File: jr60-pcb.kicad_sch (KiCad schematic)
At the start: 21 parts, among them J1 AVR-ISP-6, SW1 SW_Push, U1 ATmega32U4-A, U2 PRTR5V0U2X, X1 XTAL

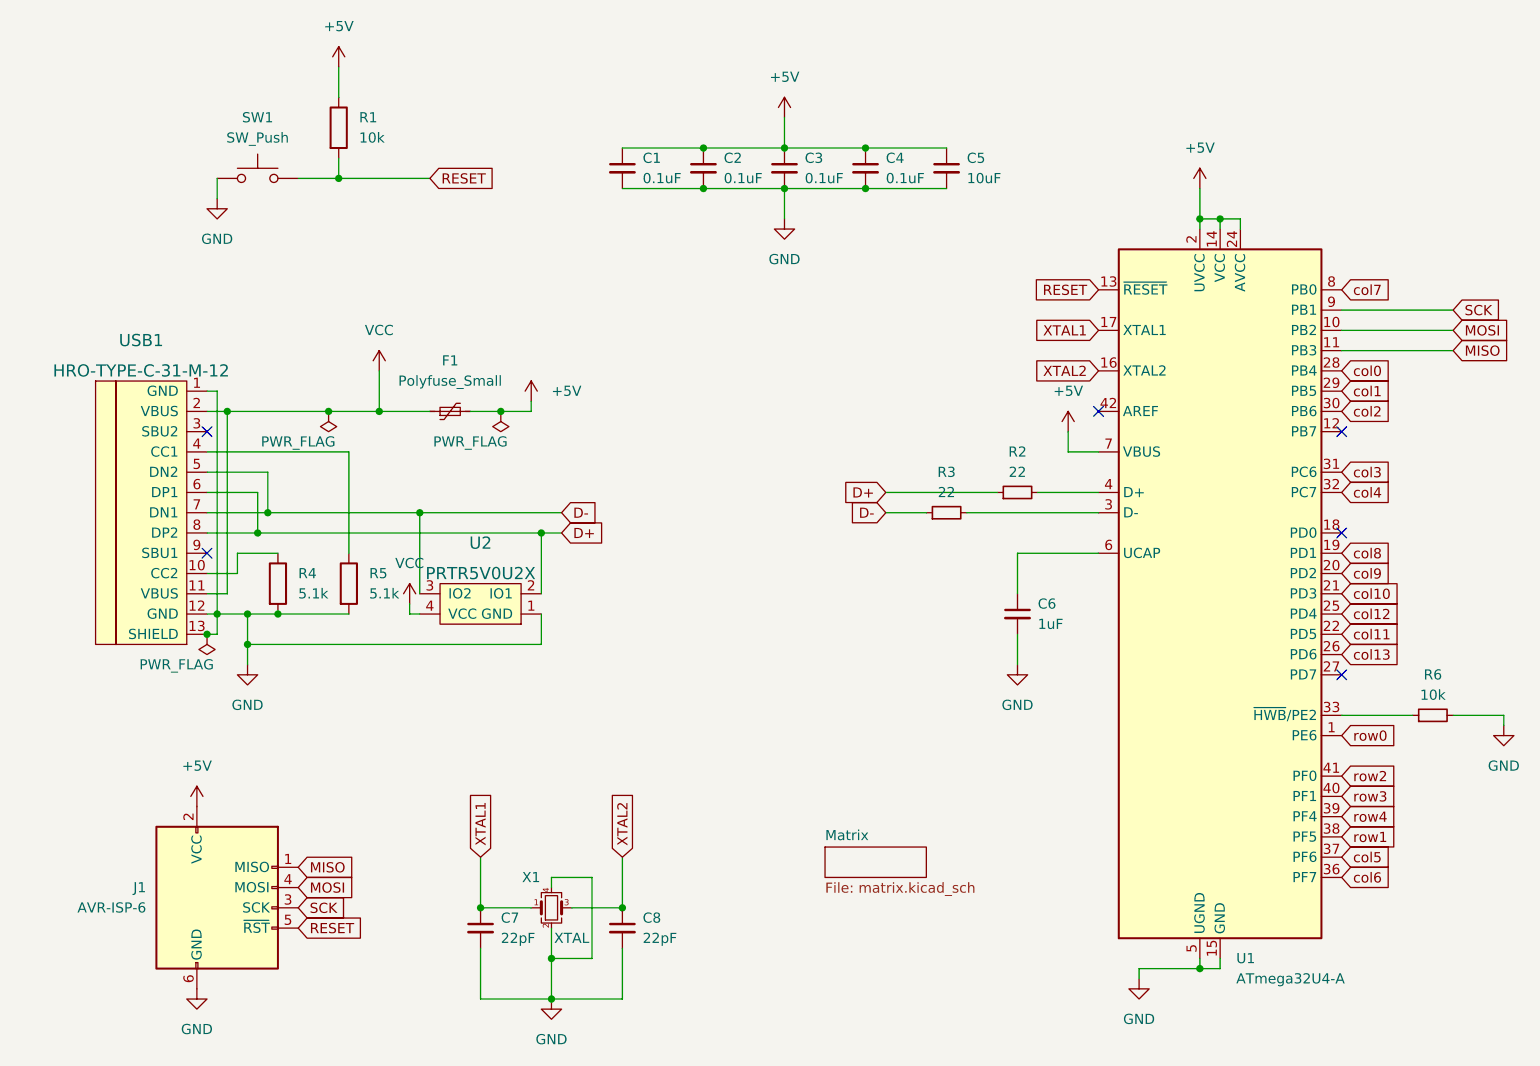
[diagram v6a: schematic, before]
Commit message: added all traces
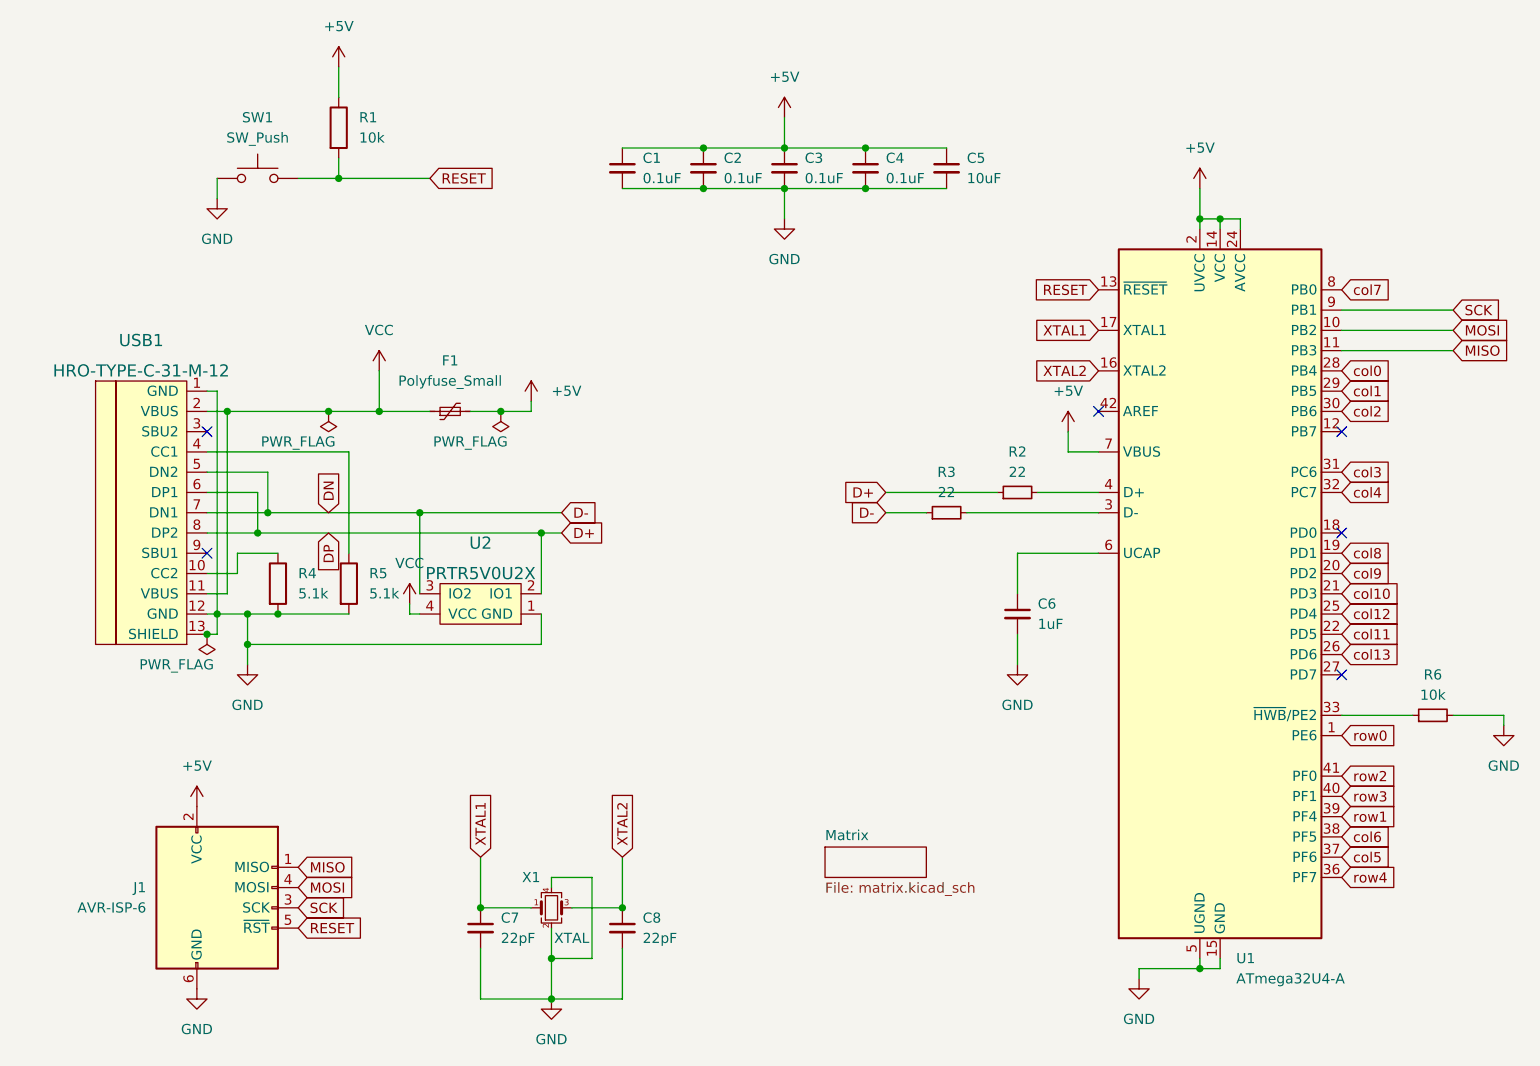
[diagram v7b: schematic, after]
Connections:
- net col6: now also U1.38 (PF5); no longer U1.36 (PF7)
- net row1: now also U1.39 (PF4); no longer U1.38 (PF5)
- net row4: now also U1.36 (PF7); no longer U1.39 (PF4)
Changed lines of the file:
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@@
     (stroke (width 0) (type default) (color 0 0 0 0))
   )
+  (global_label "DN" (shape input) (at 128.27 95.25 90) (fields_autoplaced)
+    (effects (font (size 1.27 1.27)) (justify left))
+    (property "Intersheet References" "${INTERSHEET_REFS}" (id 0) (at 128.1906 90.2364 90)
+      (effects (font (size 1.27 1.27)) (justify left) hide)
+    )
+  )
   (global_label "col5" (shape input) (at 255.27 138.43 0) (fields_autoplaced)
     (effects (font (size 1.27 1.27)) (justify left))
@@
     )
   )
-  (global_label "row4" (shape input) (at 255.27 133.35 0) (fields_autoplaced)
+  (global_label "row1" (shape input) (at 255.27 133.35 0) (fields_autoplaced)
     (effects (font (size 1.27 1.27)) (justify left))
     (property "Intersheet References" "${INTERSHEET_REFS}" (id 0) (at 262.1583 133.2706 0)
@@
     )
   )
-  (global_label "row1" (shape input) (at 255.27 135.89 0) (fields_autoplaced)
-    (effects (font (size 1.27 1.27)) (justify left))
-    (property "Intersheet References" "${INTERSHEET_REFS}" (id 0) (at 262.1583 135.8106 0)
+  (global_label "col6" (shape input) (at 255.27 135.89 0) (fields_autoplaced)
+    (effects (font (size 1.27 1.27)) (justify left))
+    (property "Intersheet References" "${INTERSHEET_REFS}" (id 0) (at 261.7955 135.8106 0)
       (effects (font (size 1.27 1.27)) (justify left) hide)
     )
@@
     )
   )
-  (global_label "col6" (shape input) (at 255.27 140.97 0) (fields_autoplaced)
-    (effects (font (size 1.27 1.27)) (justify left))
-    (property "Intersheet References" "${INTERSHEET_REFS}" (id 0) (at 261.7955 140.8906 0)
+  (global_label "row4" (shape input) (at 255.27 140.97 0) (fields_autoplaced)
+    (effects (font (size 1.27 1.27)) (justify left))
+    (property "Intersheet References" "${INTERSHEET_REFS}" (id 0) (at 262.1583 140.8906 0)
       (effects (font (size 1.27 1.27)) (justify left) hide)
     )
@@
     )
   )
+  (global_label "DP" (shape input) (at 128.27 97.79 270) (fields_autoplaced)
+    (effects (font (size 1.27 1.27)) (justify right))
+    (property "Intersheet References" "${INTERSHEET_REFS}" (id 0) (at 128.1906 102.7431 90)
+      (effects (font (size 1.27 1.27)) (justify right) hide)
+    )
+  )
